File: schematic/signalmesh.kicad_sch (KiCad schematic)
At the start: 85 parts, among them J1 FPGA I/O, J10 INA219_CONFIG, J11 INA219_CONFIG, J12 AAM_DBG, J13 DSM_DBG, J14 ACM_DBG, J2 FPGA I/O, J4 TDM_DBG, J5 INA219_CONFIG, J6 INA219_CONFIG, J7 INA219_CONFIG, J8 FPGA I/O, J9 FPGA I/O, U1 NUCLEO-H753ZI, U10 INA219AxD, U11 INA219AxD, U12 INA219AxD, U13 INA219AxD, U14 W25Q128JVS, U15 AP2112K-3.3, U16 74HC4050D, U2 NUCLEO-H753ZI, U3 NUCLEO-F303RE, U4 YAAJ_BluePill_Part_Like, U5 24LC256-I_SN, U6 BME280, U7 INA219AxD, U8 24LC256-I_SN, U9 NUCLEO-F446RE

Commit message: display driver schematic piece
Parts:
- removed U2: NUCLEO-H753ZI, NUCLEO-H753ZI:MODULE_NUCLEO-H753ZI, symbol NUCLEO-H753ZI:NUCLEO-H753ZI
- added C7: 0.1uf, Capacitor_SMD:C_0201_0603Metric, symbol Device:C_Small
- added D19, D20: LED_PWR, LED_SMD:LED_Kingbright_KPBD-3224, symbol Device:LED
- added J15: INA219_CONFIG, Connector_PinHeader_1.00mm:PinHeader_1x02_P1.00mm_Horizontal, symbol Connector_Generic:Conn_01x02
- added J3: LCD_display, Connector_PinHeader_1.00mm:PinHeader_1x04_P1.00mm_Horizontal, symbol Connector_Generic:Conn_01x04
- added R1, R2: 300, Resistor_SMD:R_0805_2012Metric_Pad1.20x1.40mm_HandSolder, symbol Device:R
- added R3, R4: 10k, Resistor_SMD:R_0805_2012Metric_Pad1.20x1.40mm_HandSolder, symbol Device:R
- added U17: NUCLEO-H753ZI, NUCLEO-H753ZI:MODULE_NUCLEO-H753ZI, symbol NUCLEO-H753ZI:NUCLEO-H753ZI
- added U18, U19, U2: HDSP-7503, Display_7Segment:HDSP-A151, symbol Display_Character:HDSP-7503
- added U20: INA219AxD, Package_SO:SOIC-8_3.9x4.9mm_P1.27mm, symbol Sensor_Energy:INA219AxD
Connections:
- net AAM_FMC_A14 is gone; now on net AAM_FMC_NWE: J1.19 (Pin_19), J8.19 (Pin_19)
- net AAM_FMC_A15 is gone; now on net AAM_FMC_NOE: J1.20 (Pin_20), J8.20 (Pin_20)
- net AAM_FMC_A17 is gone; now on net AAM_FMC_NL: J1.22 (Pin_22), J8.22 (Pin_22)
- net AAM_FMC_A18 is gone; now on net AAM_FMC_NBL0: J1.23 (Pin_23), J8.23 (Pin_23)
- net AAM_FMC_A19 is gone; now on net AAM_FMC_NBL1: J1.24 (Pin_24), J8.24 (Pin_24)
- net AAM_FMC_A2 is gone; now on net ACM_CMD_TX: J1.7 (Pin_7), J8.7 (Pin_7)
- net AAM_FMC_A3 is gone; now on net ACM_CMD_RX: J1.8 (Pin_8), J8.8 (Pin_8)
- net AAM_FMC_A4 is gone; now on net ACM_LED_PWR: J1.9 (Pin_9), J8.9 (Pin_9)
- net AAM_FMC_A5 is gone; now on net ACM_LED_FAIL: J1.10 (Pin_10), J8.10 (Pin_10)
- net AAM_FMC_A6 is gone; now on net ACM_LED_OK: J1.11 (Pin_11), J8.11 (Pin_11)
- net AAM_FMC_A7 is gone; now on net ACM_LED_WARN: J1.12 (Pin_12), J8.12 (Pin_12)
- net AAM_FMC_A8 is gone; now on net AAM_FMC_CLK: J1.13 (Pin_13), J8.13 (Pin_13)
- net ACM_FMC_D10 is gone; now on net AAM_FMC_D13: J2.14 (Pin_14), J9.14 (Pin_14)
- net ACM_FMC_D11 is gone; now on net ACM_FMC_D14: J2.15 (Pin_15), J9.15 (Pin_15)
- net ACM_FMC_D12 is gone; now on net ACM_FMC_D15: J2.16 (Pin_16), J9.16 (Pin_16)
- net ACM_FMC_D8 is gone; now on net AAM_FMC_D11: J2.12 (Pin_12), J9.12 (Pin_12)
- net ACM_FMC_D9 is gone; now on net AAM_FMC_D12: J2.13 (Pin_13), J9.13 (Pin_13)
- net 5V_TDM: now also C7.2, U20.5 (VS)
- net 5V_UUM: now also U20.8 (IN+)
- net AAM_FMC_D0: now also J2.1 (Pin_1), J9.1 (Pin_1), U1.CN12_46 (PD14); no longer J2.4 (Pin_4), J9.4 (Pin_4), U1.CN7_14 (D11/SPI_A_MOSI/TIM_E_PWM1)
- net AAM_FMC_D1: now also J2.2 (Pin_2), J9.2 (Pin_2), U1.CN12_48 (PD15); no longer J2.5 (Pin_5), J9.5 (Pin_5), U1.CN7_16 (D10/SPI_A_CS/TIM_B_PWM3)
- net AAM_FMC_D2: now also J2.3 (Pin_3), J9.3 (Pin_3), U1.CN11_57 (PD0); no longer J2.6 (Pin_6), J9.6 (Pin_6), U1.CN9_27 (D66/CAN_TX)
- net AAM_FMC_D3: now also J2.4 (Pin_4), J9.4 (Pin_4), U1.CN11_55 (PD1); no longer J2.7 (Pin_7), J9.7 (Pin_7), U1.CN9_25 (D67/CAN_RX)
- net AAM_FMC_D4: now also J2.5 (Pin_5), J9.5 (Pin_5), U1.CN12_44 (PE7); no longer J2.8 (Pin_8), J9.8 (Pin_8), U1.CN10_16 (D0/USART_A_RX), U1.CN10_20 (D41/TIMER_A_ETR)
- net AAM_FMC_D5: now also J2.6 (Pin_6), J9.6 (Pin_6), U1.CN12_40 (PE8); no longer J2.9 (Pin_9), J9.9 (Pin_9), U1.CN10_18 (D42/TIMER_A_PWM1N)
- net AAM_FMC_D6: now also J2.7 (Pin_7), J9.7 (Pin_7), U1.CN12_52 (PE9); no longer J2.10 (Pin_10), J9.10 (Pin_10), U1.CN10_4 (D6/TIMER_A_PWM1)
- net AAM_FMC_D7: now also J2.8 (Pin_8), J9.8 (Pin_8), U1.CN12_47 (PE10); no longer J2.11 (Pin_11), J9.11 (Pin_11), U1.CN10_24 (D40/TIMER_A_PWM2N)
- net AAM_FMC_NOE: now also U1.CN11_39 (PD4); no longer J2.2 (Pin_2), J9.2 (Pin_2), U1.CN9_8 (D54/USART_B_RTS)
- net AAM_FMC_NWE: now also U1.CN11_41 (PD5); no longer J2.1 (Pin_1), J9.1 (Pin_1), U1.CN9_6 (D53/USART_B_TX)
- net AAM_VDD: now also J3.1 (Pin_1)
- net ACM_CMD_RX: no longer J1.4 (Pin_4), J8.4 (Pin_4)
- net ACM_CMD_TX: no longer J1.3 (Pin_3), J8.3 (Pin_3)
- net ACM_DBG_RX: now also J1.6 (Pin_6), J8.6 (Pin_6); no longer J1.2 (Pin_2), J8.2 (Pin_2)
- net ACM_DBG_TX: now also J1.5 (Pin_5), J8.5 (Pin_5); no longer J1.1 (Pin_1), J8.1 (Pin_1)
- net ACM_FMC_D14: now also U1.CN11_69 (PD9); no longer J2.19 (Pin_19), J9.19 (Pin_19)
- net ACM_FMC_D15: now also U1.CN12_65 (PD10); no longer J2.20 (Pin_20), J9.20 (Pin_20)
- net ACM_LED_FAIL: no longer J1.6 (Pin_6), J8.6 (Pin_6)
- net ACM_LED_PWR: no longer J1.5 (Pin_5), J8.5 (Pin_5)
- net ACM_SPI_CS: now also J1.1 (Pin_1), J8.1 (Pin_1)
- net ACM_SPI_MISO: now also J1.4 (Pin_4), J8.4 (Pin_4)
- net ACM_SPI_MOSI: now also J1.2 (Pin_2), J8.2 (Pin_2)
- net ACM_SPI_SCLK: now also J1.3 (Pin_3), J8.3 (Pin_3)
- net GND: now also U4.39 (GND), C7.1, D19.1 (K), D20.1 (K), J3.4 (Pin_4), R3.1, R4.1, U18.1 (CC), U18.6 (CC), U19.1 (CC), U19.6 (CC), U2.1 (CC), U2.6 (CC), U20.6 (GND)
- net TDM_I2C1_SCL: now also U20.4 (SCL)
- net TDM_I2C1_SDA: now also U20.3 (SDA)
- net VDD_UUM: now also R2.2, U20.7 (IN-)
- net AAM_FMC_NL: now reaches U1.CN11_21 (PB7)
- net AAM_FMC_CLK: now reaches U1.CN11_40 (PD3)
- net AAM_FMC_NBL1: now reaches U1.CN11_61 (PE1)
- net AAM_FMC_D13: now reaches U1.CN12_10 (PD8)
- net AAM_FMC_D9: now reaches U1.CN12_49 (PE12)
- net AAM_FMC_D9: now also J2.10 (Pin_10), J9.10 (Pin_10)
- net AAM_FMC_D11: now reaches U1.CN12_51 (PE14)
- net AAM_FMC_D12: now reaches U1.CN12_53 (PE15)
- net AAM_FMC_D10: now reaches U1.CN12_55 (PE13)
- net AAM_FMC_D10: now also J2.11 (Pin_11), J9.11 (Pin_11)
- net AAM_FMC_D8: now reaches U1.CN12_56 (PE11)
- net AAM_FMC_D8: now also J2.9 (Pin_9), J9.9 (Pin_9)
- net AAM_FMC_NBL0: now reaches U1.CN12_64 (PE0)
- net at U4.10 (PA15): now also U2.2 (F)
- net at U4.11 (PB3): now also U2.4 (E)
- net at U4.12 (PB4): now also U2.5 (D)
- net at U4.13 (PB5): now also U2.8 (C)
- net at U4.14 (PB6): now also U2.9 (B)
- net at U4.15 (PB7): now also U2.10 (A)
- net at U4.16 (PB8): now also U18.7 (DP)
- net at U4.17 (PB9): now also U18.3 (G)
- net 5V_7SDD: now reaches U4.18 (5V)
- net at U4.23 (PC14): now also U18.2 (F)
- net at U4.24 (PC15): now also U18.4 (E)
- net at U4.25 (PA0): now also U18.5 (D)
- net at U4.26 (PA1): now also U18.8 (C)
- net at U4.27 (PA2): now also U18.9 (B)
- net at U4.28 (PA3): now also U18.10 (A)
- net at U4.29 (PA4): now also U19.7 (DP)
- net at U4.30 (PA5): now also U19.3 (G)
- net at U4.31 (PA6): now also U19.2 (F)
- net at U4.32 (PA7): now also U19.4 (E)
- net at U4.33 (PB0): now also U19.5 (D)
- net at U4.34 (PB1): now also U19.8 (C)
- net at U4.35 (PB10): now also U19.9 (B)
- net at U4.36 (PB11): now also U19.10 (A)
- net at U4.8 (PA11): now also U2.7 (DP)
- net at U4.9 (PA12): now also U2.3 (G)
- net AAM_FMC_A0: no longer names the net of J2.21 (Pin_21), J9.21 (Pin_21)
- net AAM_FMC_A1: no longer names the net of J2.22 (Pin_22), J9.22 (Pin_22)
- net AAM_FMC_A10: no longer names the net of J1.15 (Pin_15), J8.15 (Pin_15)
- net AAM_FMC_A11: no longer names the net of J1.16 (Pin_16), J8.16 (Pin_16)
- net AAM_FMC_A12: no longer names the net of J1.17 (Pin_17), J8.17 (Pin_17)
- net AAM_FMC_A13: no longer names the net of J1.18 (Pin_18), J8.18 (Pin_18)
- net AAM_FMC_A16 renamed AAM_FMC_NE
- net AAM_FMC_NE: now also U1.CN12_19 (PC7)
- net AAM_FMC_A9: no longer names the net of J1.14 (Pin_14), J8.14 (Pin_14)
- removed net AAM_FMC_NCE: J2.3 (Pin_3), J9.3 (Pin_3), U1.CN12_19 (PC7)
- net ACM_FMC_D13: no longer names the net of J9.17 (Pin_17)
- new net: D20.2 (A), R2.1
- new net: J15.1 (Pin_1), J15.2 (Pin_2), R3.2, R4.2, U20.1 (A1), U20.2 (A0)
- new net: D19.2 (A), R1.1
- new net: U17.CN11_10 (NC), U17.CN11_26 (NC), U17.CN11_67 (NC)
- new net: U17.CN11_19 (GND_CN11), U17.CN11_20 (GND_CN11), U17.CN11_22 (GND_CN11), U17.CN11_49 (GND_CN11), U17.CN11_60 (GND_CN11), U17.CN11_71 (GND_CN11), U17.CN11_72 (GND_CN11), U17.CN11_8 (GND_CN11)
- new net: U17.CN12_20 (GND_CN12), U17.CN12_39 (GND_CN12), U17.CN12_54 (GND_CN12), U17.CN12_63 (GND_CN12), U17.CN12_71 (GND_CN12), U17.CN12_72 (GND_CN12), U17.CN12_9 (GND_CN12)
- new net: J2.19 (Pin_19), J9.19 (Pin_19)
- new net: J2.20 (Pin_20), J9.20 (Pin_20)
- new net: U17.CN8_11 (GND_CN8), U17.CN8_13 (GND_CN8)
- new net: U17.CN10_17 (GND_CN10), U17.CN10_22 (GND_CN10), U17.CN10_27 (GND_CN10), U17.CN10_5 (GND_CN10)
- new net: U17.CN9_12 (GND_CN9), U17.CN9_23 (GND_CN9)
- new net 7SDD_VDD: R1.2
- new net AAM_I2C1_SCL: J3.3 (Pin_3)
- new net AAM_I2C1_SDA: J3.2 (Pin_2)
- no-connect marks 0 -> 10
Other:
- note added: "7-Segment Display Driver (7SDD)"
- note added: "AAM -> DSM Record"
- note added: "Data Siphon Module"
- note added: "Driver MCU for a 3 digit 7 segment display.Ideally audio engine settings can be displayed through here live"
- note added: "INA219 7SDD"
- note added: "STM32H753 NUCLEO"
- moved on the sheet: C6, D10, D11, D12, D13, D14, D15, D16, D17, D18, J1, J12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

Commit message: updating FMC pins
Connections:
- net ACM_LED_PWR is gone; now on net ACM_LED_FAIL: J1.9 (Pin_9), J8.9 (Pin_9)
- net AAM_DBG_RX: now also U1.CN11_4 (PD2)
- net AAM_DBG_TX: now also U1.CN11_3 (PC12)
- net AAM_FMC_CLK: now also J1.18 (Pin_18), J8.18 (Pin_18); no longer J1.13 (Pin_13), J8.13 (Pin_13)
- net ACM_LED_FAIL: no longer J1.10 (Pin_10), J8.10 (Pin_10)
- net ACM_LED_OK: now also J1.10 (Pin_10), J8.10 (Pin_10); no longer J1.11 (Pin_11), J8.11 (Pin_11)
- net ACM_LED_WARN: now also J1.11 (Pin_11), J8.11 (Pin_11); no longer J1.12 (Pin_12), J8.12 (Pin_12)
- net DSM_DBG_RX: now also U17.CN11_4 (PD2)
- net DSM_DBG_TX: now also U17.CN11_3 (PC12)
- new net: J1.12 (Pin_12), J8.12 (Pin_12)
- new net: J1.13 (Pin_13), J8.13 (Pin_13)
- no-connect marks 10 -> 9
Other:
- moved on the sheet: U17A, U17B, U17C, U17D, U17E, U17F

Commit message: UUM SPI flash. gpio ctrl with 74lvc
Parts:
- added C8, C9: 10uf, Capacitor_SMD:C_0201_0603Metric, symbol Device:C_Small
- added D21, D25, D26: LED_PWR, LED_SMD:LED_Kingbright_KPBD-3224, symbol Device:LED
- added D22: LED_OK, LED_SMD:LED_Kingbright_KPBD-3224, symbol Device:LED
- added D23: LED_FAIL, LED_SMD:LED_Kingbright_KPBD-3224, symbol Device:LED
- added D24: LED_WARN, LED_SMD:LED_Kingbright_KPBD-3224, symbol Device:LED
- added J16: DSM_DBG, Connector_PinHeader_1.00mm:PinHeader_1x03_P1.00mm_Horizontal, symbol Connector_Generic:Conn_01x03
- added J17: LCD_display, Connector_PinHeader_1.00mm:PinHeader_1x04_P1.00mm_Horizontal, symbol Connector_Generic:Conn_01x04
- added R10, R5, R6, R7, R8, R9: 300, Resistor_SMD:R_0805_2012Metric_Pad1.20x1.40mm_HandSolder, symbol Device:R
- added R42: 100, Resistor_SMD:R_0805_2012Metric_Pad1.20x1.40mm_HandSolder, symbol Device:R
- added U21, U24: 74HC4050D, 74HC4050D:SO16, symbol 74HC4050D:74HC4050D
- added U22, U25: AP2112K-3.3, Package_TO_SOT_SMD:SOT-23-5, symbol Regulator_Linear:AP2112K-3.3
- added U23, U26: W25Q128JVS, Package_SO:SOIC-8_5.3x5.3mm_P1.27mm, symbol Memory_Flash:W25Q128JVS
- added U27: MCP2551-I-P, Package_DIP:DIP-8_W7.62mm, symbol Interface_CAN_LIN:MCP2551-I-P
- added U28: 74LVC1G3157, symbol 74xGxx:74LVC1G3157
- added unit 6 of U3
- added unit 5 of U3
- added unit 1 of U3
- added unit 3 of U3
- added unit 4 of U3
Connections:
- net 5V_7SDD: now also U20.8 (IN+)
- net 5V_AAM: now also U1.CN11_18 (5V), U17.CN11_18 (5V)
- net 5V_UUM: no longer U20.8 (IN+)
- net AAM_DAC_L: now also U1.CN12_11 (PA5), U17.CN12_11 (PA5)
- net AAM_DAC_R: now also U1.CN11_32 (PA4), U17.CN11_32 (PA4)
- net AAM_INTRPT_TX: now also U1.CN11_62 (PE6), U17.CN11_47 (PE3)
- net DSM_DBG_RX: now also J16.2 (Pin_2)
- net DSM_DBG_TX: now also J16.1 (Pin_1)
- net GND: now also U1.CN11_19 (GND_CN11), U1.CN11_20 (GND_CN11), U1.CN11_22 (GND_CN11), U1.CN11_49 (GND_CN11), U1.CN11_60 (GND_CN11), U1.CN11_71 (GND_CN11), U1.CN11_72 (GND_CN11), U1.CN11_8 (GND_CN11), U17.CN11_19 (GND_CN11), U17.CN11_20 (GND_CN11), U17.CN11_22 (GND_CN11), U17.CN11_49 (GND_CN11), U17.CN11_60 (GND_CN11), U17.CN11_71 (GND_CN11), U17.CN11_72 (GND_CN11), U17.CN11_8 (GND_CN11), C8.2, C9.2, D21.1 (K), D22.1 (K), D23.1 (K), D24.1 (K), D25.1 (K), D26.1 (K), J16.3 (Pin_3), J17.4 (Pin_4), U21.11 (5A), U21.14 (6A), U21.8 (GND), U22.2 (GND), U23.4 (GND), U24.11 (5A), U24.14 (6A), U24.8 (GND), U25.2 (GND), U26.4 (GND), U28.2 (GND)
- net VDD_UUM: now also U22.1 (VIN), U22.3 (EN), U25.1 (VIN), U25.3 (EN); no longer R2.2, U20.7 (IN-)
- net UUM_SPI1_SCK: now reaches U3.CN10_11 (PA5)
- net UUM_SPI1_MISO: now reaches U3.CN10_13 (PA6)
- net UUM_SPI1_MISO: now also U28.3
- net UUM_SPI1_MOSI: now reaches U3.CN10_15 (PA7)
- net UUM_SPI1_MOSI: now also U21.7 (3A), U24.7 (3A)
- net UUM_SPI1_CS: now reaches U3.CN10_23 (PA8)
- net UUM_SPI1_CS: now also U21.3 (1A), U24.3 (1A)
- net UUM_CAN_RD: now reaches U3.CN10_3 (PB8)
- net UUM_DBG_TX: now reaches U3.CN10_35 (PA2)
- net UUM_DBG_RX: now reaches U3.CN10_37 (PA3)
- net UUM_CAN_TD: now reaches U3.CN10_5 (PB9)
- net AAM_INTRPT_RX: now reaches U1.CN11_47 (PE3)
- net AAM_INTRPT_RX: now also U17.CN11_62 (PE6)
- net 7SDD_CMD_TX: now reaches U4.6 (PA9)
- net 7SDD_CMD_RX: now reaches U4.7 (PA10)
- new net: U24.10 (4Y), U26.2 (DO/IO_{1})
- new net: U24.2 (1Y), U26.1 (~{CS})
- new net: U24.4 (2Y), U26.6 (CLK)
- new net: U24.6 (3Y), U26.5 (DI/IO_{0})
- new net: D21.2 (A), R5.1
- new net: D22.2 (A), R6.1
- new net: D24.2 (A), R8.1
- new net: D26.2 (A), R10.2
- new net: U21.2 (1Y), U23.1 (~{CS})
- new net: U21.10 (4Y), U23.2 (DO/IO_{1})
- new net: U21.6 (3Y), U23.5 (DI/IO_{0})
- new net: U21.4 (2Y), U23.6 (CLK)
- new net: C8.1, R9.1, U22.5 (VOUT), U23.8 (VCC)
- new net: U3.CN7_19 (GND_S1), U3.CN7_20 (GND_S1), U3.CN7_22 (GND_S1), U3.CN7_8 (GND_S1)
- new net: C9.1, R10.1, U25.5 (VOUT), U26.8 (VCC)
- new net: R42.1, U28.5 (VCC)
- new net: D23.2 (A), R7.1
- new net: D25.2 (A), R9.2
- new net: U3.CN6_6 (GND), U3.CN6_7 (GND)
- new net 3V3_UUM: R42.2, U21.1 (VCC), U23.3 (~{WP}/IO_{2}), U23.7 (~{HOLD}/~{RESET}/IO_{3}), U24.1 (VCC), U26.3 (~{WP}/IO_{2}), U26.7 (~{HOLD}/~{RESET}/IO_{3}), U3.CN7_16 (+3V3_S1)
- new net DSM_I2C1_SCL: J17.3 (Pin_3)
- new net DSM_I2C1_SDA: J17.2 (Pin_2)
- new net DSM_LED_FAIL: R8.2
- new net DSM_LED_OK: R6.2
- new net DSM_LED_WARN: R7.2
- new net DSM_VDD: J17.1 (Pin_1), R5.2
- new net UUM_SPI1_MISO_A: U21.9 (4A), U28.6
- new net UUM_SPI1_MISO_B: U24.9 (4A), U28.1
- new net UUM_SPI1_SCLK: U21.5 (2A), U24.5 (2A)
- new net UUM_SPI_SEL: U28.4, U3.CN7_25 (PC14)
- new net VDD_7SDD: R2.2, U20.7 (IN-)
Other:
- note added: "UUM CAN DBG"
- note added: "UUM writes to both SPI flashes at once but can only read from 1 at a time via a GPIO-ctrl'd switch"
- note added: "W25Q128 UUM #1"
- note added: "W25Q128 UUM #2"
- moved on the sheet: C6, D10, D11, D12, D13, D14, D19, J1, J13, J14, J2, R1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

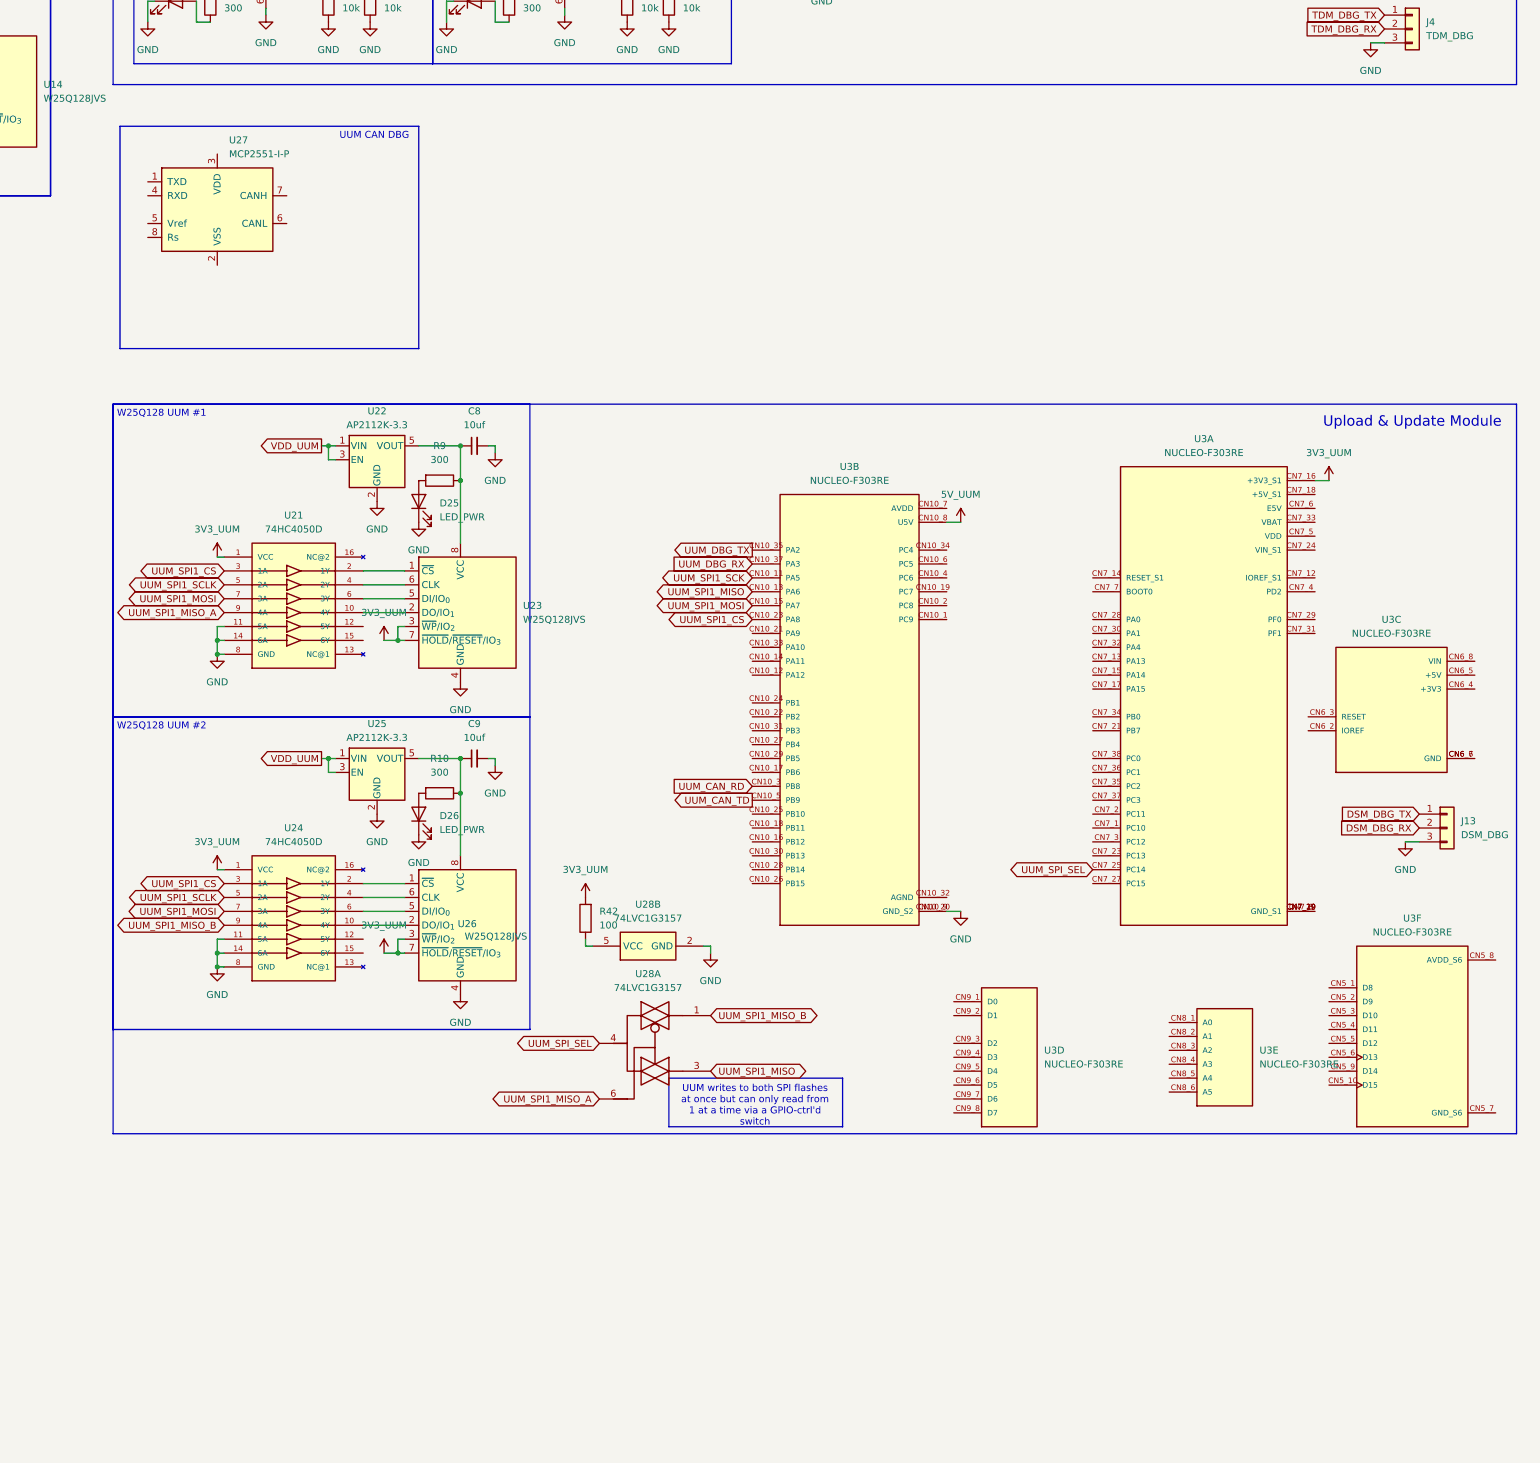
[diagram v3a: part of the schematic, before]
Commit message: add CAN tranceivers
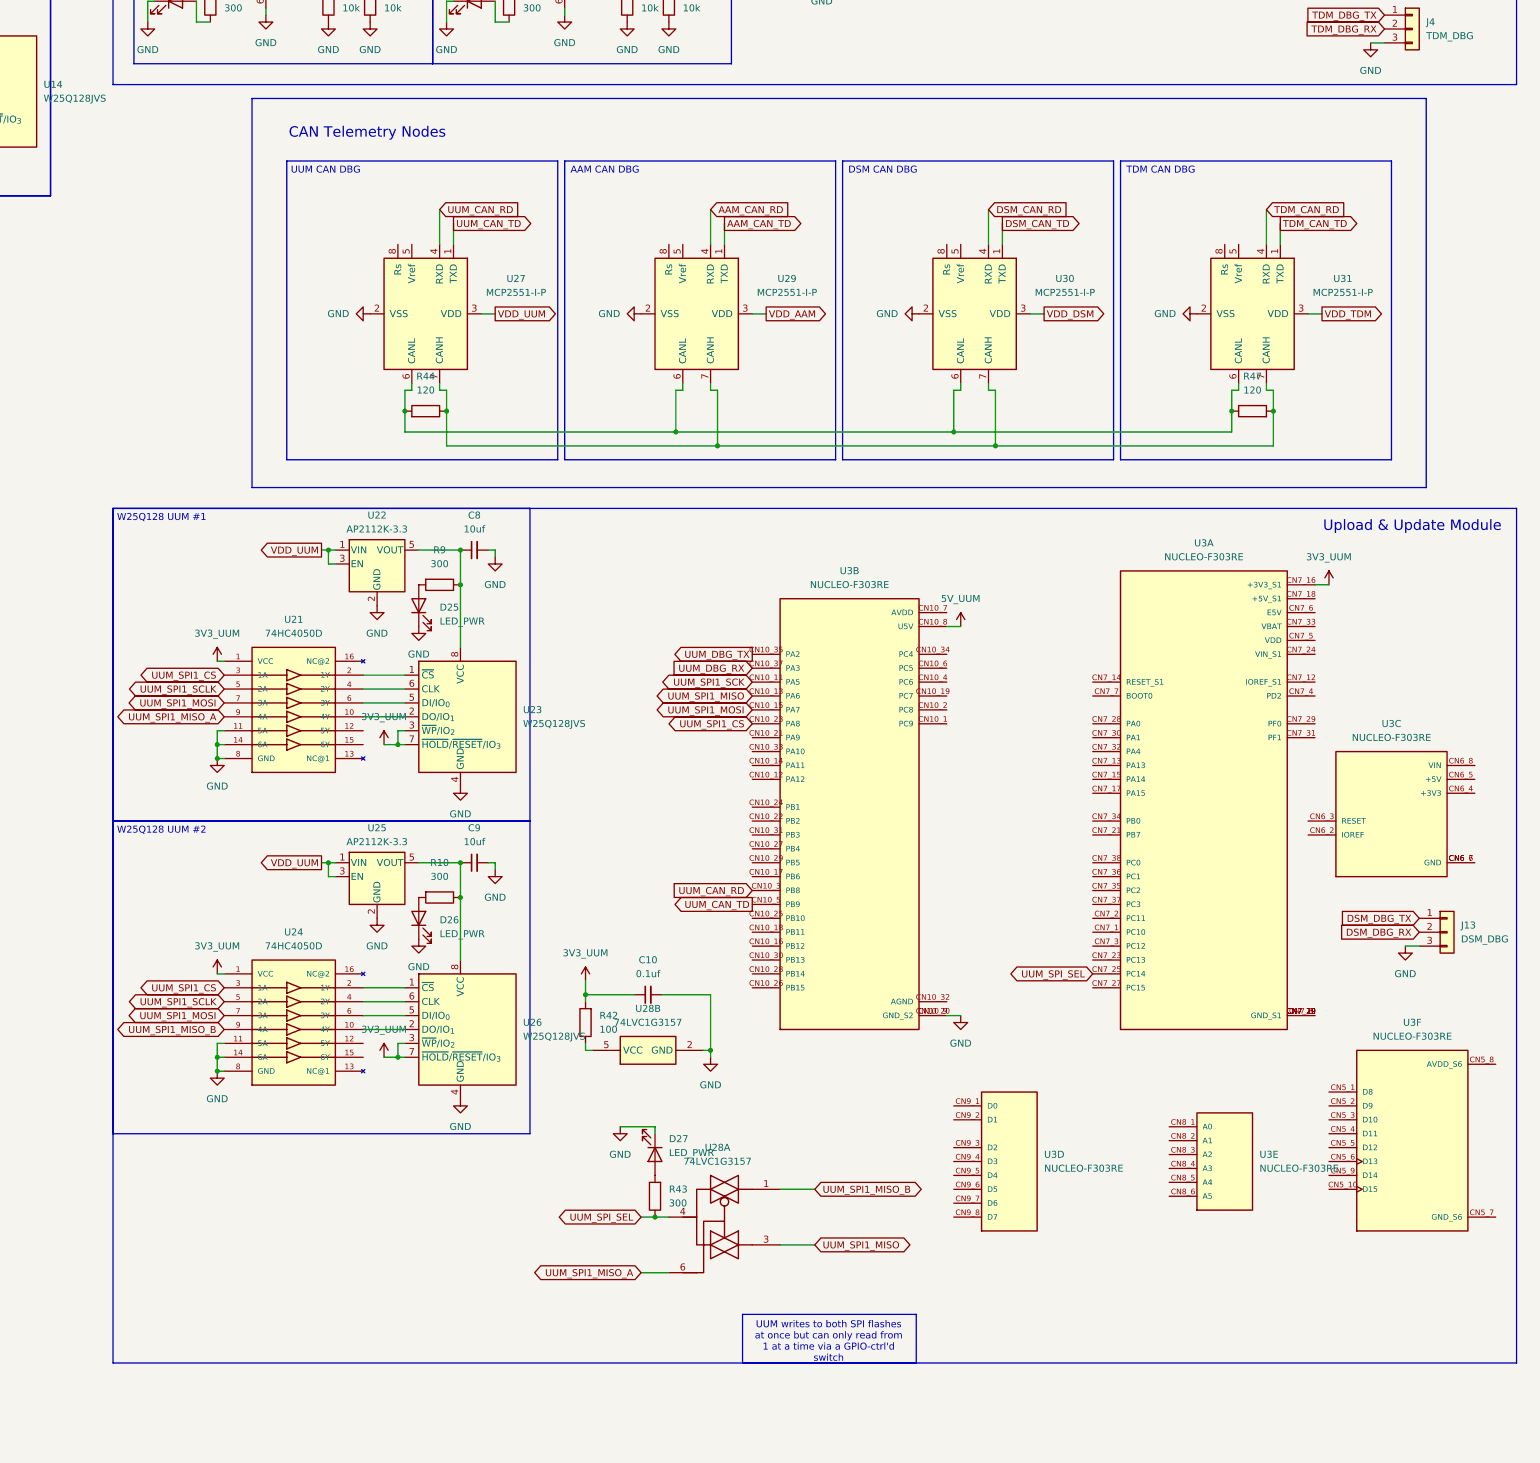
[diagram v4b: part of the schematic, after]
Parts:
- added C10: 0.1uf, Capacitor_SMD:C_0201_0603Metric, symbol Device:C_Small
- added D27: LED_PWR, LED_SMD:LED_Kingbright_KPBD-3224, symbol Device:LED
- added R43: 300, Resistor_SMD:R_0805_2012Metric_Pad1.20x1.40mm_HandSolder, symbol Device:R
- added R44, R47: 120, Resistor_SMD:R_0805_2012Metric_Pad1.20x1.40mm_HandSolder, symbol Device:R
- added U29, U30, U31: MCP2551-I-P, Package_DIP:DIP-8_W7.62mm, symbol Interface_CAN_LIN:MCP2551-I-P
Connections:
- net 3V3_UUM: now also C10.1
- net GND: now also U27.2 (VSS), C10.2, D27.1 (K), U29.2 (VSS), U30.2 (VSS), U31.2 (VSS)
- net UUM_CAN_RD: now also U27.4 (RXD)
- net UUM_CAN_TD: now also U27.1 (TXD)
- net UUM_SPI_SEL: now also R43.1
- net VDD_AAM: now also U29.3 (VDD)
- net VDD_DSM: now also U30.3 (VDD)
- net VDD_UUM: now also U27.3 (VDD)
- net at U27.6 (CANL): now also R44.2, R47.1, U29.6 (CANL), U30.6 (CANL), U31.6 (CANL)
- net at U27.7 (CANH): now also R44.1, R47.2, U29.7 (CANH), U30.7 (CANH), U31.7 (CANH)
- new net: D27.2 (A), R43.2
- new net AAM_CAN_RD: U29.4 (RXD)
- new net AAM_CAN_TD: U29.1 (TXD)
- new net DSM_CAN_RD: U30.4 (RXD)
- new net DSM_CAN_TD: U30.1 (TXD)
- new net TDM_CAN_RD: U31.4 (RXD)
- new net TDM_CAN_TD: U31.1 (TXD)
- new net VDD_TDM: U31.3 (VDD)
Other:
- note added: "AAM CAN DBG"
- note added: "CAN Telemetry Nodes"
- note added: "DSM CAN DBG"
- note added: "TDM CAN DBG"
- moved on the sheet: C8, C9, D25, D26, J13, R10, R42, R9, U21, U22, U23, U24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

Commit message: CAN rework
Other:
- note added: "AAM CAN TLM"
- note added: "DSM CAN TLM"
- note added: "TDM CAN TLM"
- note added: "UUM CAN TLM"
- note removed: "AAM CAN DBG"
- note removed: "DSM CAN DBG"
- note removed: "TDM CAN DBG"
- note removed: "UUM CAN DBG"
- moved on the sheet: C10, C8, C9, D19, D25, D26, D27, J13, R1, R10, R42, R43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

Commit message: PCB updates
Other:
- moved on the sheet: D19, R1, U18, U19, U2, U4
